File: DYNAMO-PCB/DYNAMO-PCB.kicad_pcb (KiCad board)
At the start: 2 copper layers, 208.9 x 129.5 mm, 34 parts, among them J10 Conn_01x03_Pin, J11 Conn_01x03_Pin, J12 Conn_01x03_Pin, J33 Conn_02x05_Counter_Clockwise, J5 Conn_01x02_Pin, J6 Conn_01x03_Pin, J7 Conn_01x08_Socket, J8 Conn_01x03_Pin, J9 Conn_01x03_Pin

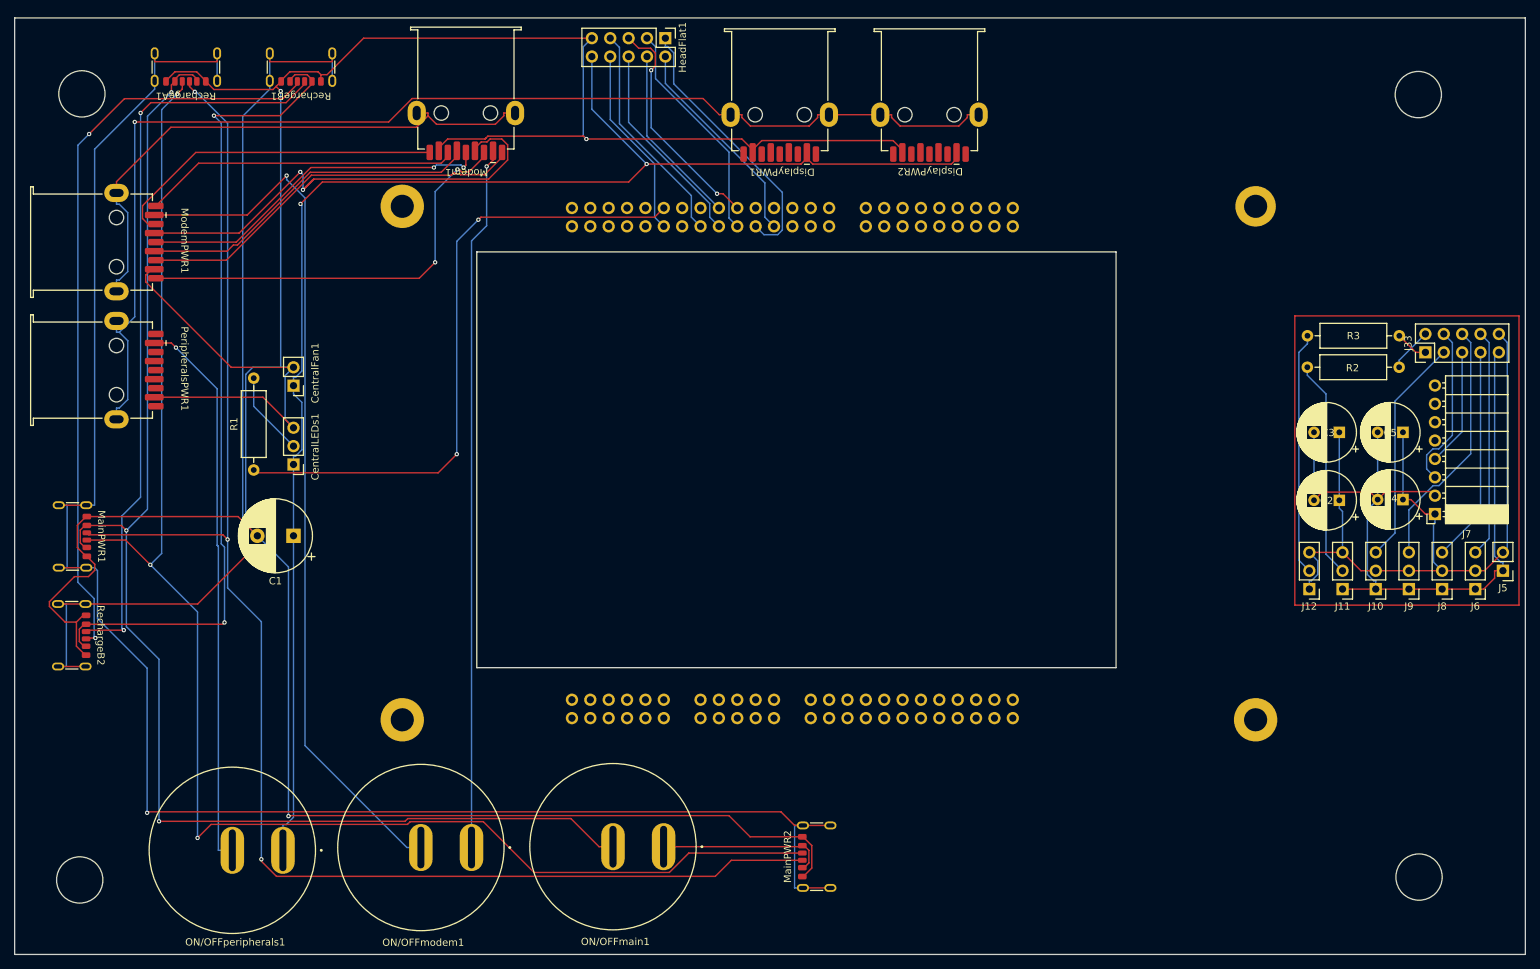
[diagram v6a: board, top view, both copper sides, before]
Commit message: more compact
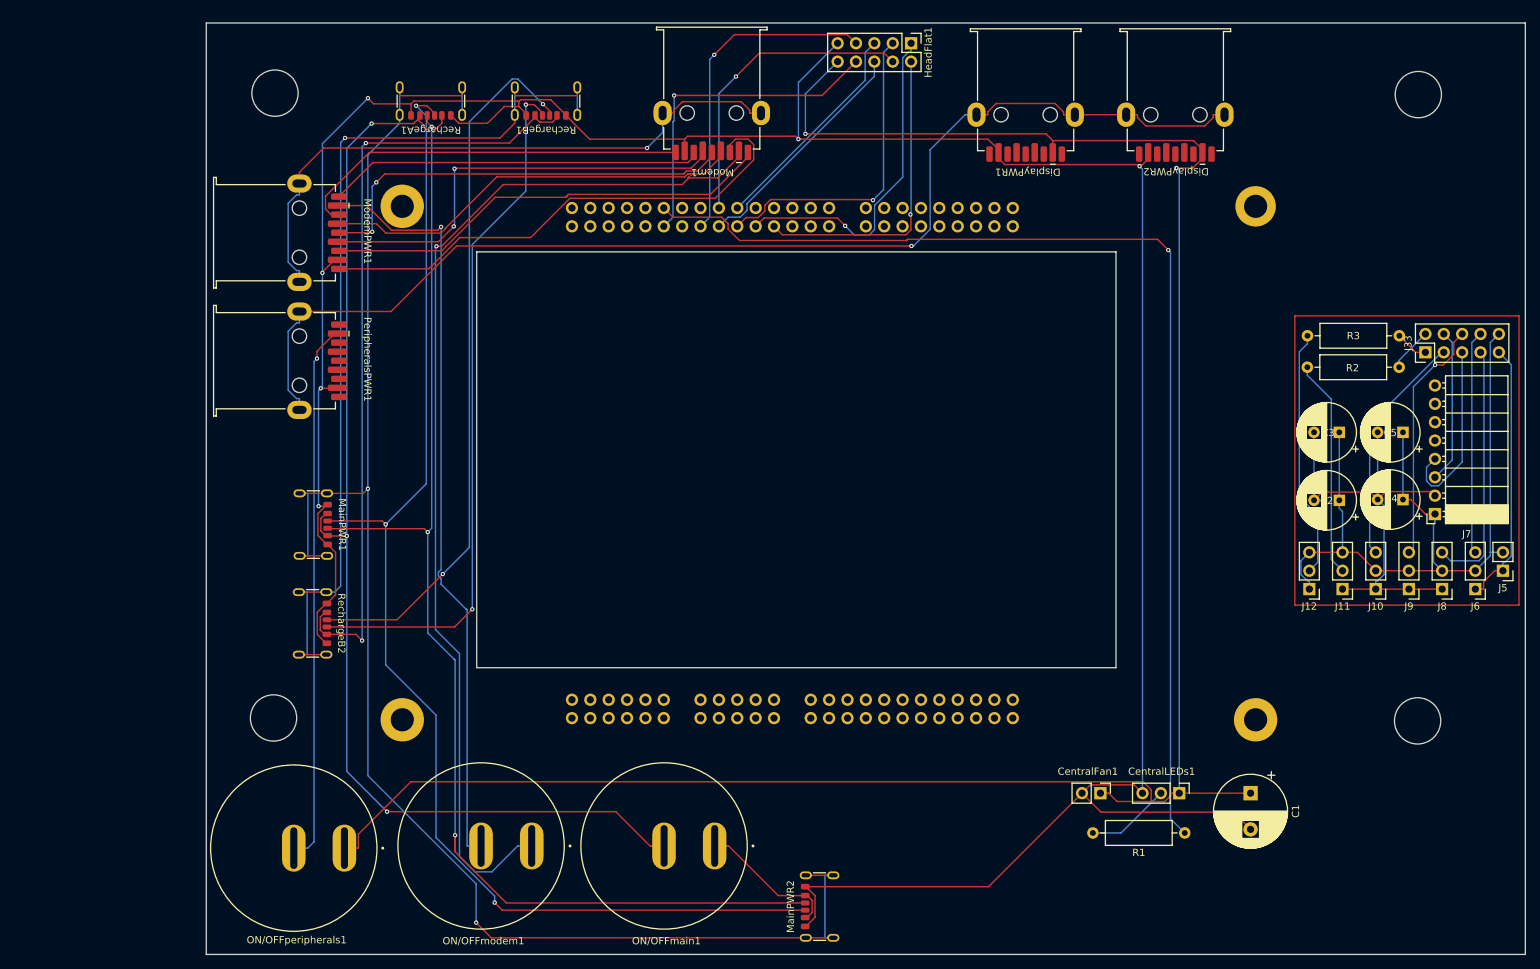
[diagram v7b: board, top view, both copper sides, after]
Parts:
- moved R1 138.2 mm to (204.7, 138.8), turned to 180 degrees
- moved C1 137.0 mm to (213.8, 133.3), turned to -90 degrees
- moved CentralLEDs1 130.6 mm to (203.9, 133.3), turned to -90 degrees
- moved CentralFan1 125.0 mm to (193.0, 133.3), turned to -90 degrees
- moved RechargeA1 34.2 mm to (100.5, 36.5)
- moved RechargeB1 34.2 mm to (116.4, 36.5)
- moved DisplayPWR1 34.0 mm to (182.9, 36.9)
- moved DisplayPWR2 34.0 mm to (203.6, 36.9)
- moved Modem1 34.0 mm to (139.5, 36.7)
- moved HeadFlat1 34.0 mm to (166.9, 29.6)
- moved RechargeB2 33.3 mm to (83.0, 109.8)
- moved MainPWR1 33.3 mm to (83.1, 96.2)
- moved ModemPWR1 25.3 mm to (79.7, 55.6)
- moved PeripheralsPWR1 25.3 mm to (79.7, 73.3)
- moved ON/OFFperipherals1 8.51 mm to (81.5, 140.9)
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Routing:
- net /Power Distribution/+5V peripherals: track 205.8 -> 301.7 mm
- net Net-(A1A-D6): track 89.3 -> 154.5 mm, vias 2 -> 1
- net Net-(Modem1-VBUS): track 97.6 -> 146.1 mm
- net GND: track 448.2 -> 406.7 mm, vias 3 -> 6
- net Net-(MainPWR1-CC1): track 208.5 -> 174.2 mm
- net Net-(MainPWR1-CC2): track 207.9 -> 177.9 mm
- net Net-(MainPWR1-VBUS-PadA9): track 185.5 -> 158.8 mm
- net Net-(MainPWR1-SHIELD): track 248.5 -> 227.7 mm, vias 1 -> 2
- net Net-(A1A-D13): track 26.5 -> 45.8 mm, vias 0 -> 1
- net Net-(A1A-D3/SCL): track 25.1 -> 42.7 mm, vias 0 -> 1
- net Net-(ModemPWR1-VBUS): track 122.3 -> 105.5 mm
- net Net-(A1A-D11): track 31.2 -> 45.7 mm, vias 0 -> 1
- net Net-(A1A-D7): track 29.7 -> 43.0 mm, vias 0 -> 1
- net Net-(Modem1-D-): track 72.2 -> 59.1 mm, vias 2 -> 0
- net Net-(Modem1-D+): track 48.1 -> 60.8 mm, vias 0 -> 2
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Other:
- board size 208.9 x 129.5 mm -> 182.4 x 128.8 mm

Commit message: track width 0.2 --> 0.5
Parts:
- moved C1 2.37 mm to (211.7, 132.2)
- moved CentralFan1 2.37 mm to (190.9, 132.2)
- moved CentralLEDs1 2.37 mm to (201.8, 132.2)
- moved R1 2.37 mm to (202.6, 137.7)
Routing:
- net Net-(A1A-D9): track 43.6 -> 98.4 mm, vias 1 -> 3
- net Net-(A1A-D11): track 45.7 -> 90.5 mm, vias 1 -> 3
- net Net-(A1A-D13): track 45.8 -> 81.1 mm, vias 1 -> 2
- net /Power Distribution/+5V peripherals: track 301.7 -> 278.9 mm, vias 2 -> 1
- net GND: track 406.7 -> 421.1 mm, vias 6 -> 5
- net Net-(DisplayPWR1-SHIELD): track 164.5 -> 178.7 mm
- net Net-(A1A-D10): track 32.7 -> 45.7 mm, vias 0 -> 1
- net Net-(MainPWR1-SHIELD): track 227.7 -> 239.2 mm, vias 2 -> 1
- net Net-(RechargeB1-SHIELD): track 127.1 -> 116.0 mm, vias 1 -> 0
- net Net-(J33-Pin_6): track 33.9 -> 44.2 mm
- net Net-(J33-Pin_8): track 30.9 -> 40.3 mm, vias 0 -> 1
- net Net-(J33-Pin_5): track 25.3 -> 16.3 mm
- net Net-(J33-Pin_4): track 21.3 -> 29.1 mm
- net Net-(Modem1-SSTX-): track 70.7 -> 63.6 mm, vias 0 -> 2
- net Net-(Modem1-VBUS): track 146.1 -> 139.5 mm
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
